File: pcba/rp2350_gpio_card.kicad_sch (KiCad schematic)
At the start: 42 parts, among them J1 Conn_01x10_Pin, J2 Conn_01x10_Pin, P1 USB_C_Plug_USB2.0, U1 AP2112K-3.3, U2 RP2350_60QFN, U3 W25Q128JVS, U4 NCP1117-3.3_SOT223, Y1 ABM8-272-T3

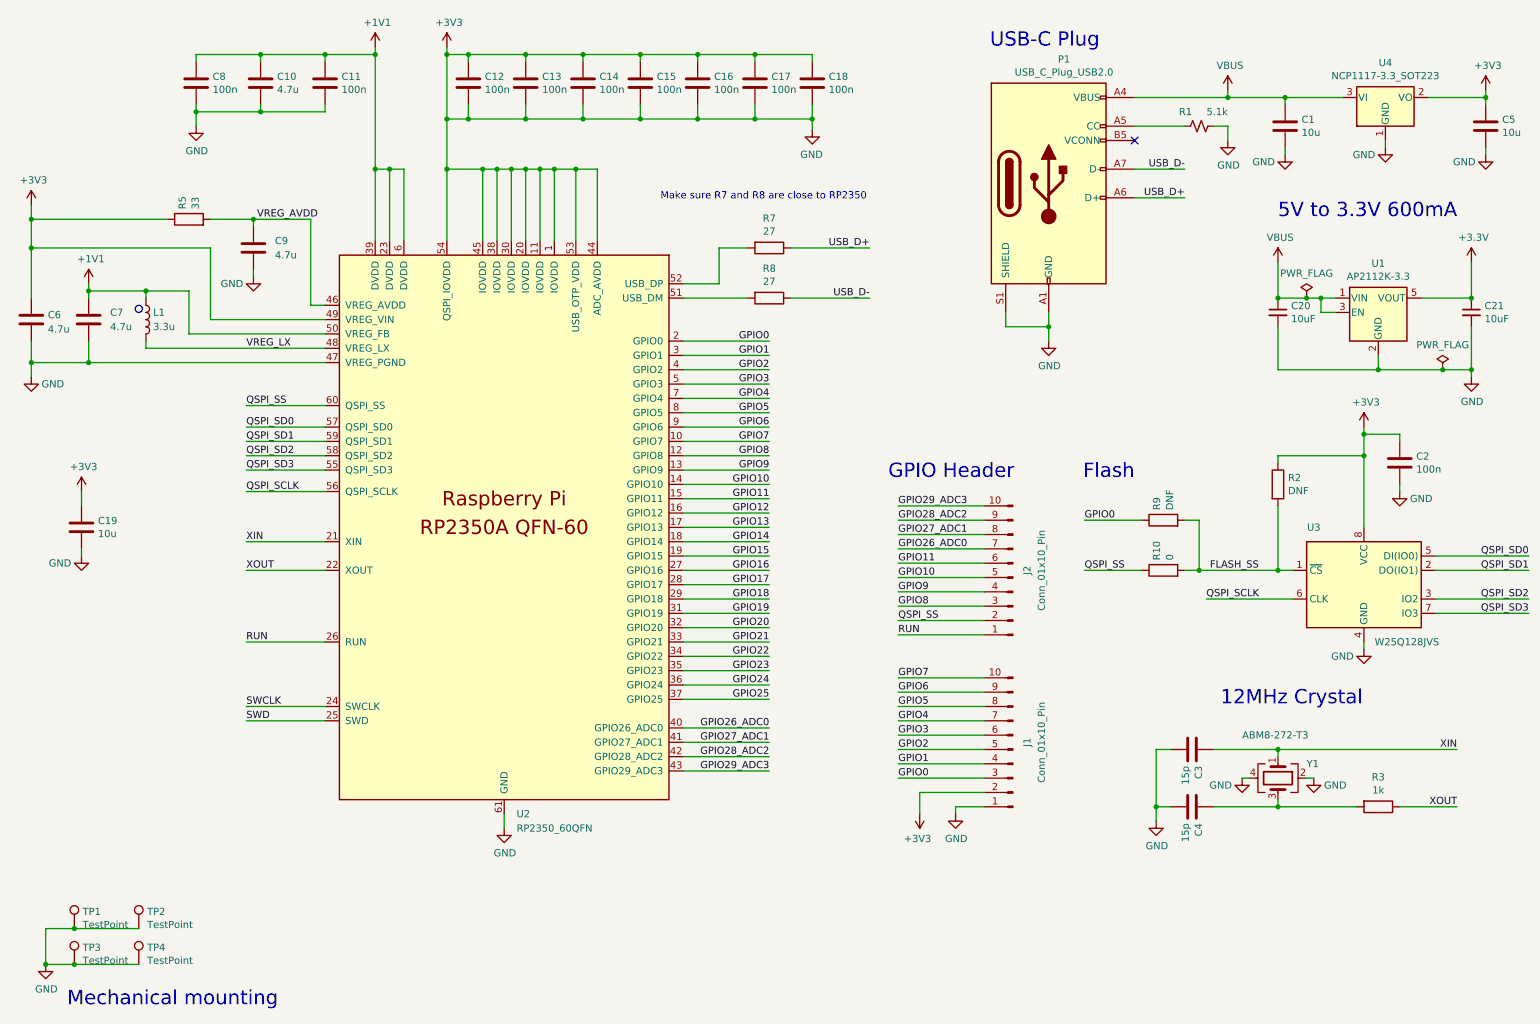
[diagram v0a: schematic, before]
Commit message: update schematics and start working on pcb (very WIP, need help)
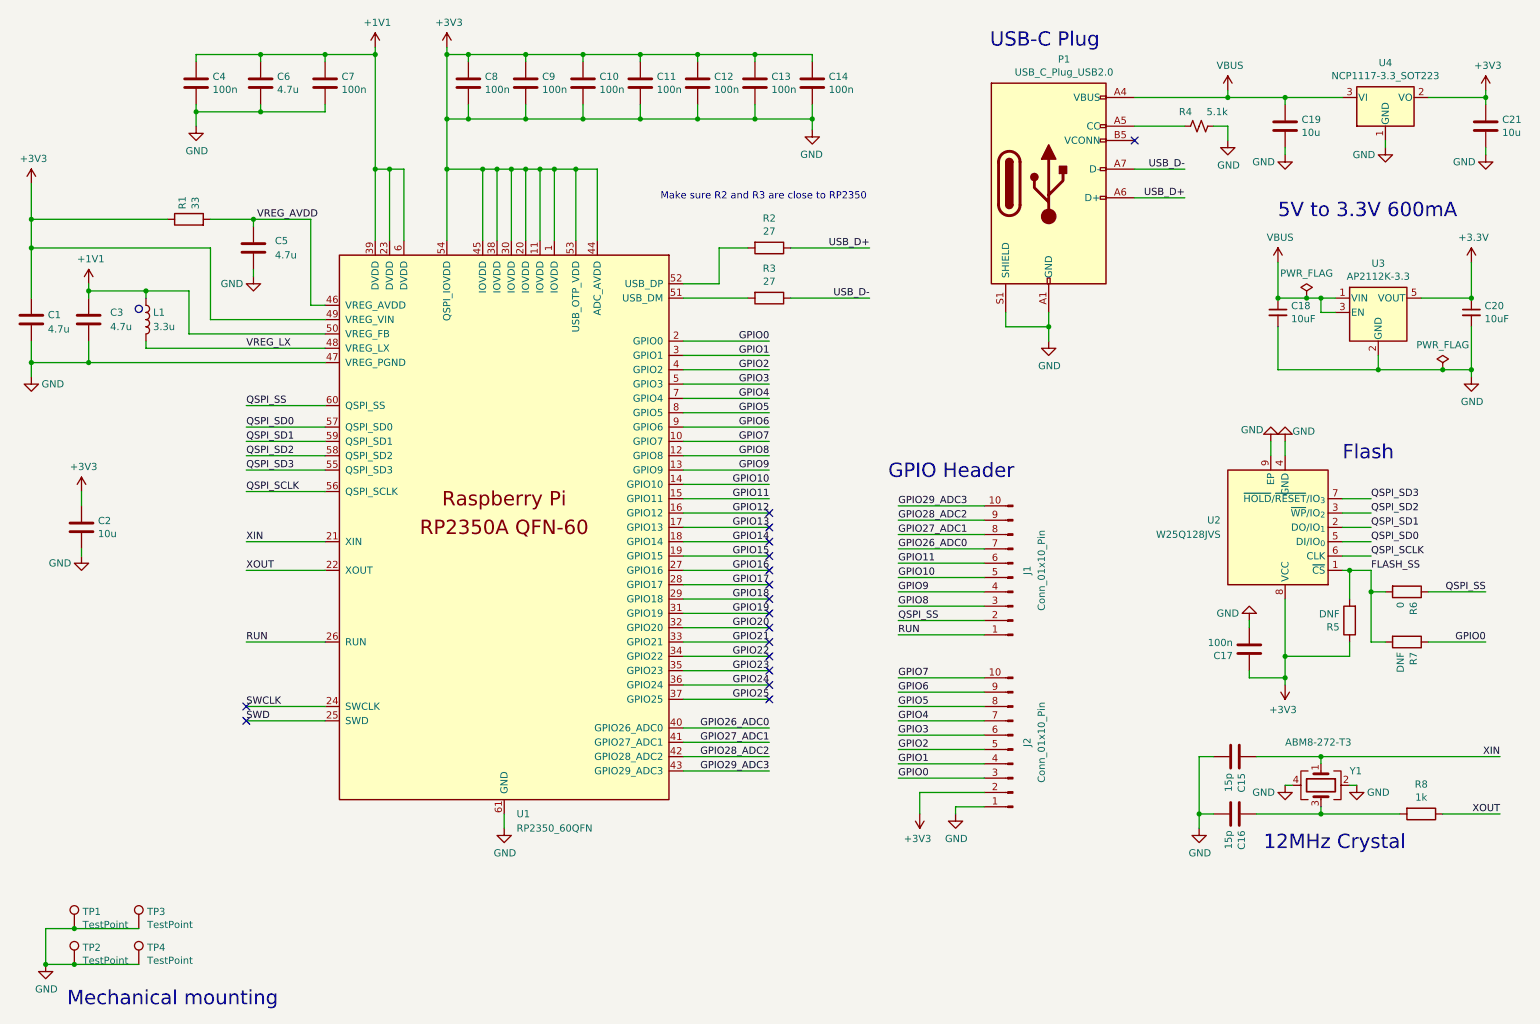
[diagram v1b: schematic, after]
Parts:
- removed C2: 100n, Capacitor_SMD:C_0402_1005Metric, symbol Device:C
- removed R10: 0, Resistor_SMD:R_0402_1005Metric, symbol Device:R
- removed R2, R9: DNF, Resistor_SMD:R_0402_1005Metric, symbol Device:R
- removed U3: W25Q128JVS, Package_SO:SOIC-8_5.23x5.23mm_P1.27mm, symbol Memory_Flash:W25Q128JVS
- added C17: 100n, Capacitor_SMD:C_0402_1005Metric, symbol Device:C
- added R5, R7: DNF, Resistor_SMD:R_0402_1005Metric, symbol Device:R
- added R6: 0, Resistor_SMD:R_0402_1005Metric, symbol Device:R
- added U2: W25Q128JVS, Package_SON:WSON-8-1EP_6x5mm_P1.27mm_EP3.4x4.3mm, symbol Memory_Flash:W25Q128JVP
- J1: renamed from J2; footprint (none) -> Connector_Harwin:Harwin_M20-89010xx_1x10_P2.54mm_Horizontal
- J2: renamed from J1; footprint (none) -> Connector_Harwin:Harwin_M20-89010xx_1x10_P2.54mm_Horizontal
- renumbered C6 to C1, C14 to C10, C15 to C11, C16 to C12, C17 to C13, C18 to C14, C3 to C15, C4 to C16, C20 to C18, C1 to C19, C19 to C2, C21 to C20, C5 to C21, C7 to C3, C8 to C4, C9 to C5, C10 to C6, C11 to C7, C12 to C8, C13 to C9, R5 to R1, R7 to R2, R8 to R3, R1 to R4, R3 to R8, TP3 to TP2, TP2 to TP3, U2 to U1, U1 to U3
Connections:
- net +3V3: now also C17.1, C17.2, R5.1, U2.4 (GND), U2.8 (VCC), U2.9 (EP)
- net FLASH_SS: now also R5.2, R6.2, R7.2, U2.1 (~{CS})
- net GPIO0: now also R7.1
- net QSPI_SCLK: now also U2.6 (CLK)
- net QSPI_SD0: now also U2.5 (DI/IO_{0})
- net QSPI_SD1: now also U2.2 (DO/IO_{1})
- net QSPI_SD2: now also U2.3 (~{WP}/IO_{2})
- net QSPI_SD3: now also U2.7 (~{HOLD}/~{RESET}/IO_{3})
- net QSPI_SS: now also R6.1
- no-connect marks 1 -> 17
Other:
- note added: "Make sure R2 and R3 are close to RP2350"
- note removed: "Make sure R7 and R8 are close to RP2350"
- title: RP2350 GPIO Card V1.0 -> RP2350 GPIO Card V1.1
- moved on the sheet: C15, C16, R8, Y1

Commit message: finish first PCB prototype, modify schematic
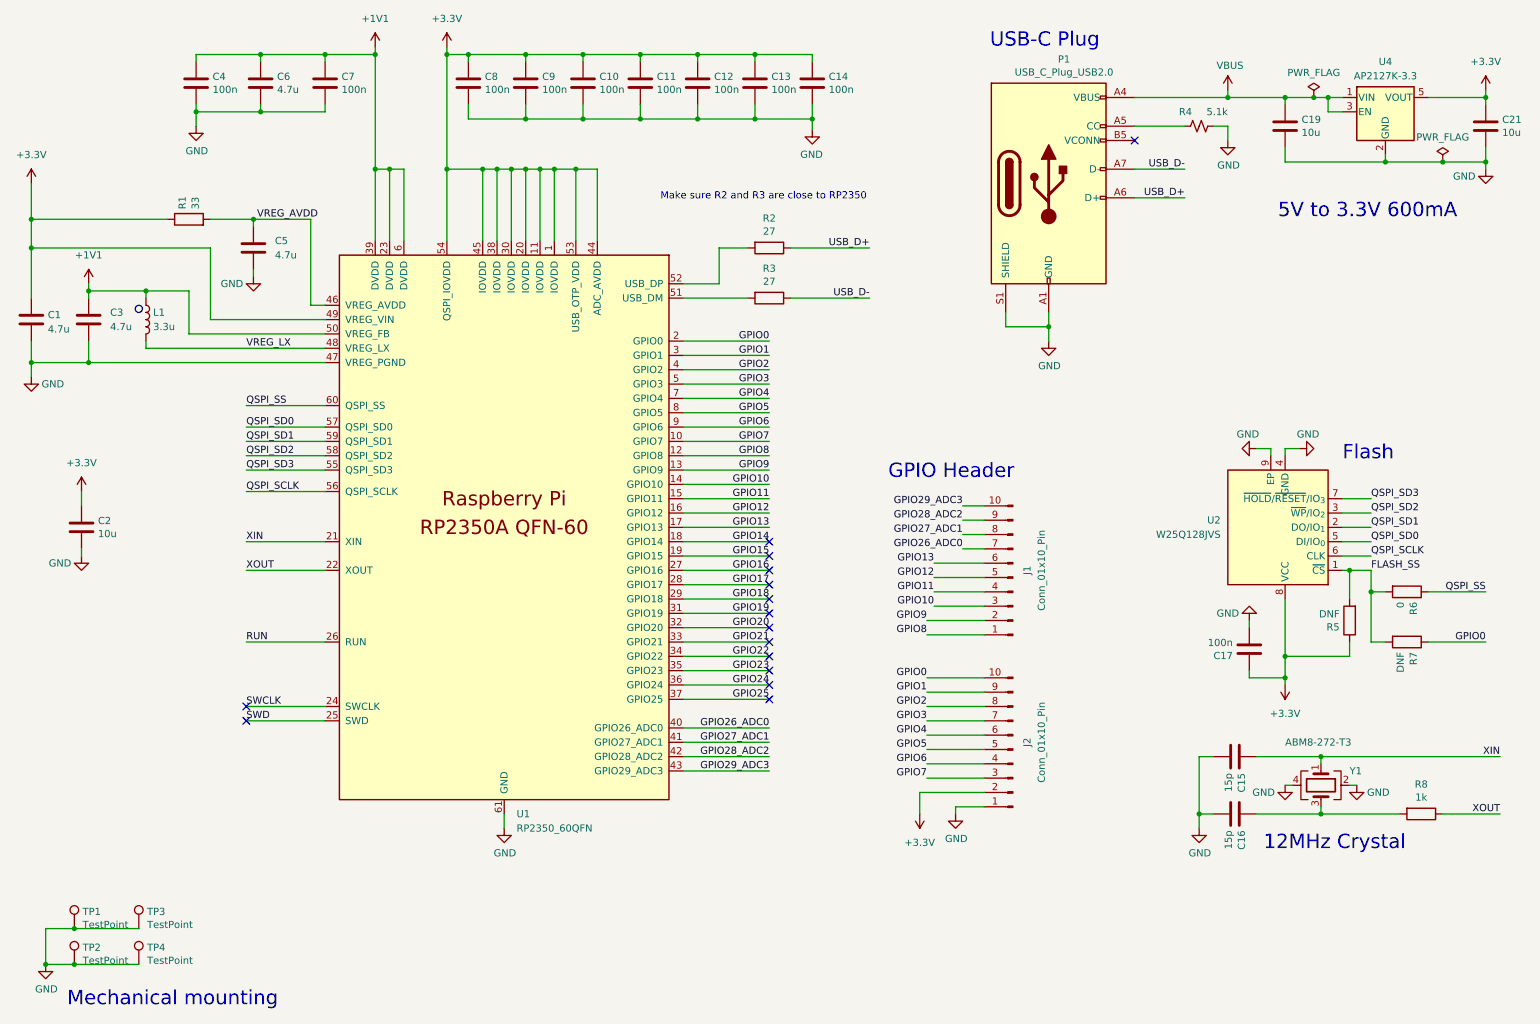
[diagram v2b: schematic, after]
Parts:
- removed C18, C20: 10uF, Capacitor_SMD:C_0805_2012Metric, symbol Device:C_Small
- removed U3: AP2112K-3.3, Package_TO_SOT_SMD:SOT-23-5, symbol Regulator_Linear:AP2112K-3.3
- removed U4: NCP1117-3.3_SOT223, Package_TO_SOT_SMD:SOT-223-3_TabPin2, symbol Regulator_Linear:NCP1117-3.3_SOT223
- added U4: AP2127K-3.3, Package_TO_SOT_SMD:SOT-23-5, symbol Regulator_Linear:AP2127K-3.3
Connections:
- net +3.3V: now also C1.1, C10.1, C11.1, C12.1, C13.1, C14.1, C17.1, C2.1, C21.1, C8.1, C9.1, J2.2 (Pin_2), R1.1, R5.1, U1.1 (IOVDD), U1.11 (IOVDD), U1.20 (IOVDD), U1.30 (IOVDD), U1.38 (IOVDD), U1.44 (ADC_AVDD), U1.45 (IOVDD), U1.49 (VREG_VIN), U1.53 (USB_OTP_VDD), U1.54 (QSPI_IOVDD), U2.8 (VCC), U4.5 (VOUT)
- net GPIO0: now also J2.10 (Pin_10); no longer J2.3 (Pin_3)
- net GPIO1: now also J2.9 (Pin_9); no longer J2.4 (Pin_4)
- net GPIO10: now also J1.3 (Pin_3); no longer J1.5 (Pin_5)
- net GPIO11: now also J1.4 (Pin_4); no longer J1.6 (Pin_6)
- net GPIO12: now also J1.5 (Pin_5)
- net GPIO13: now also J1.6 (Pin_6)
- net GPIO2: now also J2.8 (Pin_8); no longer J2.5 (Pin_5)
- net GPIO3: now also J2.7 (Pin_7); no longer J2.6 (Pin_6)
- net GPIO4: now also J2.6 (Pin_6); no longer J2.7 (Pin_7)
- net GPIO5: now also J2.5 (Pin_5); no longer J2.8 (Pin_8)
- net GPIO6: now also J2.4 (Pin_4); no longer J2.9 (Pin_9)
- net GPIO7: now also J2.3 (Pin_3); no longer J2.10 (Pin_10)
- net GPIO8: now also J1.1 (Pin_1); no longer J1.3 (Pin_3)
- net GPIO9: now also J1.2 (Pin_2); no longer J1.4 (Pin_4)
- net QSPI_SS: no longer J1.2 (Pin_2)
- net RUN: no longer J1.1 (Pin_1)
- net VBUS: now also U4.1 (VIN), U4.3 (EN)
- net +3V3 renamed GND
- net GND: now also U4.2 (GND); no longer C1.1, C10.1, C11.1, C12.1, C13.1, C14.1, C17.1, C2.1, C21.1, C8.1, C9.1, J2.2 (Pin_2), R1.1, R5.1, U1.1 (IOVDD), U1.11 (IOVDD), U1.20 (IOVDD), U1.30 (IOVDD), U1.38 (IOVDD), U1.44 (ADC_AVDD), U1.45 (IOVDD), U1.49 (VREG_VIN), U1.53 (USB_OTP_VDD), U1.54 (QSPI_IOVDD), U2.8 (VCC)
- no-connect marks 17 -> 15
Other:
- title: RP2350 GPIO Card V1.1 -> RP2350 GPIO Card V1.2.1

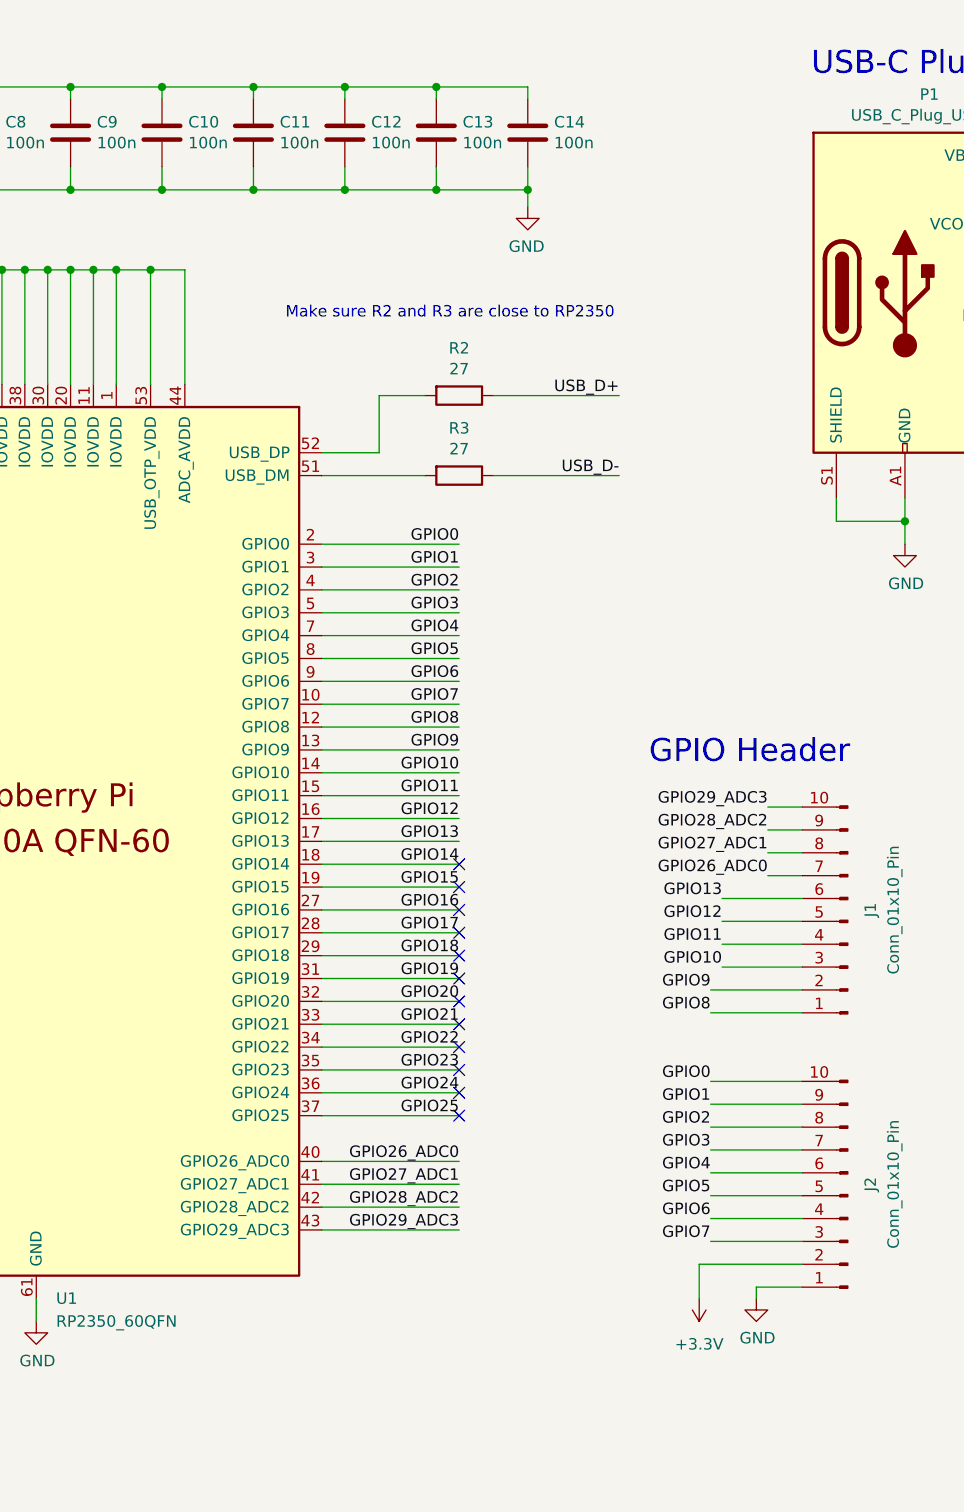
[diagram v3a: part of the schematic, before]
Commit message: change footprint, version v122
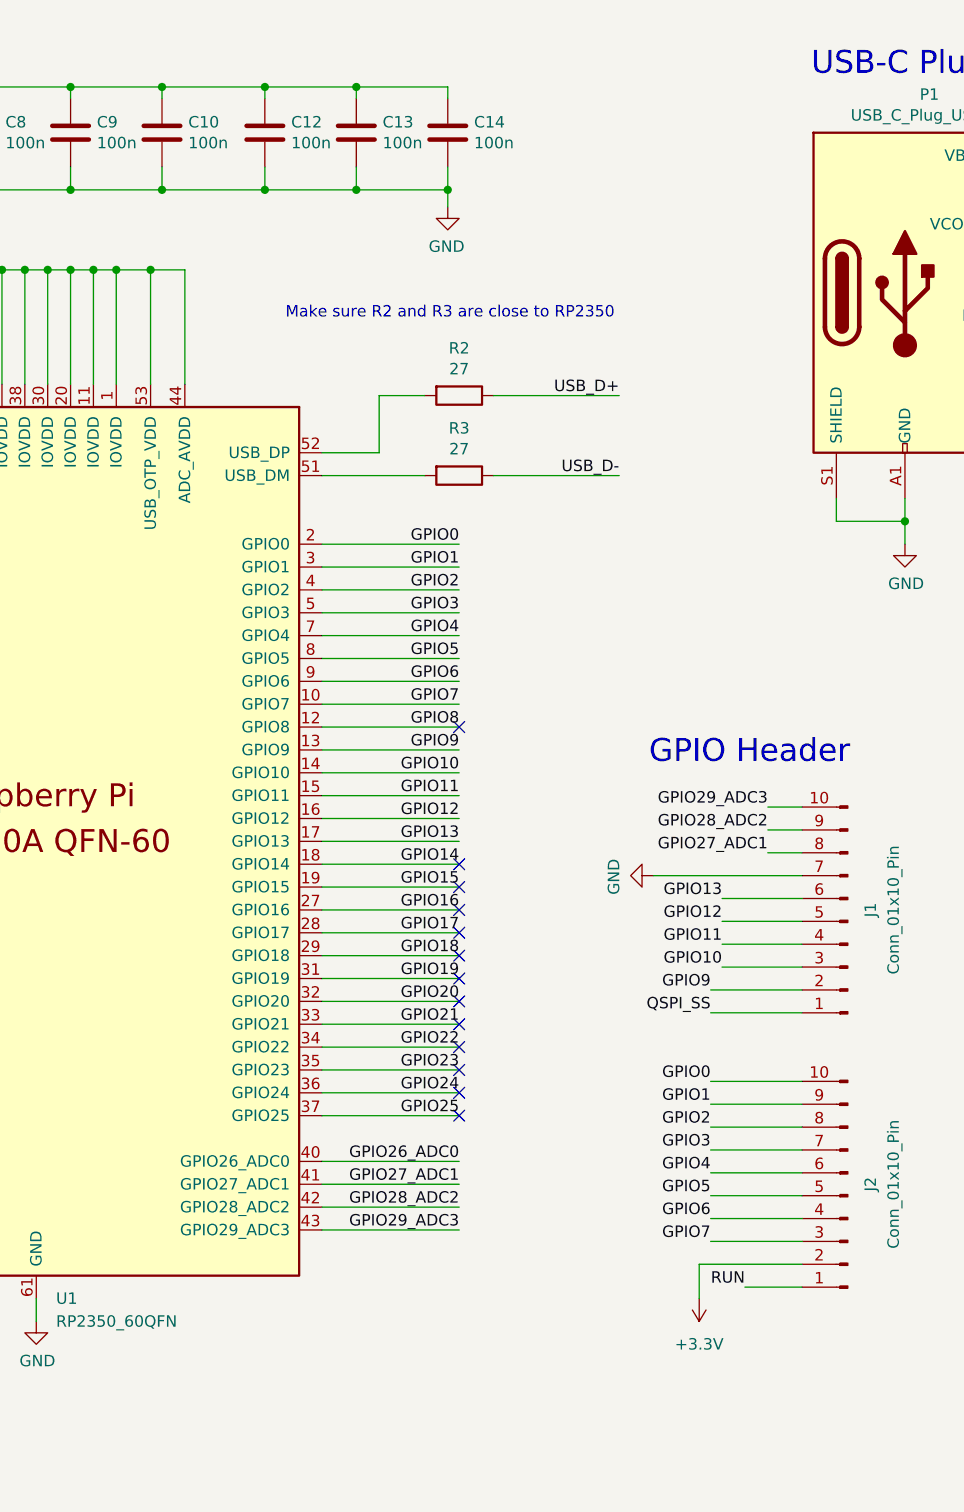
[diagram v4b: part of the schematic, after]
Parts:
- removed C11: 100n, Capacitor_SMD:C_0402_1005Metric, symbol Device:C
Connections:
- net GND: now also J1.7 (Pin_7); no longer J2.1 (Pin_1)
- net GPIO26_ADC0: no longer J1.7 (Pin_7)
- net GPIO8: no longer J1.1 (Pin_1)
- net QSPI_SS: now also J1.1 (Pin_1)
- net RUN: now also J2.1 (Pin_1)
- no-connect marks 15 -> 16
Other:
- moved on the sheet: C12, C13, C14

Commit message: fix inductor magnetism issue and rearrange several other components according to RP2350 datasheet
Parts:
- J1, J2: footprint Connector_Harwin:Harwin_M20-89010xx_1x10_P2.54mm_Horizontal -> RP2350CardCustomFootprintsLibrary:Custom_Harwin_M20-89010xx_1x10_P2.54mm_Horizontal
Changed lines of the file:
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@@
 			)
 		)
-		(property "Footprint" "Connector_Harwin:Harwin_M20-89010xx_1x10_P2.54mm_Horizontal"
+		(property "Footprint" "RP2350CardCustomFootprintsLibrary:Custom_Harwin_M20-89010xx_1x10_P2.54mm_Horizontal"
 			(at 190.5 114.3 0)
 			(effects
@@
 			)
 		)
-		(property "Footprint" "Connector_Harwin:Harwin_M20-89010xx_1x10_P2.54mm_Horizontal"
+		(property "Footprint" "RP2350CardCustomFootprintsLibrary:Custom_Harwin_M20-89010xx_1x10_P2.54mm_Horizontal"
 			(at 190.5 144.78 0)
 			(effects
